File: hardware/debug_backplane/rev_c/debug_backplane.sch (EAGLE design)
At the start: 312 parts, among them J1 BACKPLANE_CONTROLLER_MODULE_D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, J11 PJ-102AH, J12 MICRO_USB_B_HIROSE_ZX62R-B-5P, J2 BACKPLANE_GENERIC_MODULE_DEBUG, J3 BACKPLANE_GENERIC_MODULE_DEBUG, J9 MICRO_USB_B_HIROSE_ZX62R-B-5P, Q1 DMN32D2LDF, Q10 MOSFET-NCHANNELSMD, Q2 DMN32D2LDF, Q3 DMN32D2LDF, Q4 DMN32D2LDF, Q5 DMN32D2LDF, Q6 DMN32D2LDF, U1 FT232RQ, U10 LTC2943, U11 LTC2943, U12 MAX8887EZK33+T, U13 MCP23008QFN, U14 MCP23008QFN, U15 PCA9544AQFN-N20, U16 SAM4LC8AA, U17 SN74LVC2T45, U18 SN74LVC2T45, U19 SN74LVC2T45, U2 FT232RQ, U20 SN74LVC2T45, U21 TS3USB30E, U22 TS3USB30E, U23 TS3USB30E, U24 TUSB2077A, U25 LTC4360, U26 TUSB2077A, U27 FT232RQ, U28 MCP23008QFN, U29 M24C01WMN, U3 FT232RQ, U31 NCP301LSN30, U32 NCP301LSN30, U4 FT232RQ, U5 FT232RQ, U6 FXMA2102, U7 FXMA2102, U8 LTC2943, U9 LTC2943, X1 16MHz, Y1 ABMM, Y2 ABMM

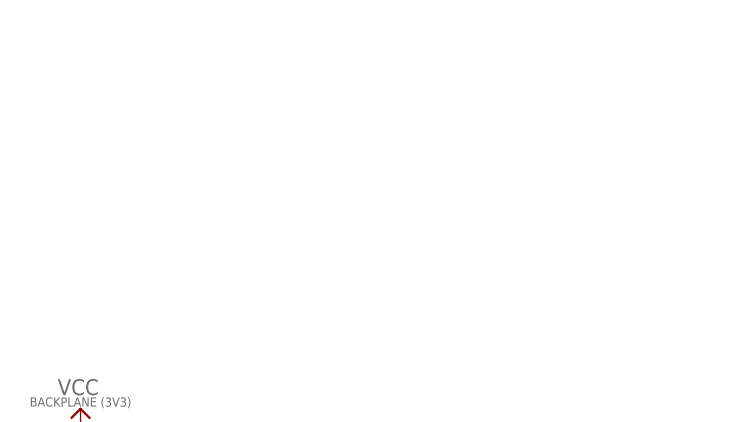
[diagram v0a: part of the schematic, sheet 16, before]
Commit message: debug_backplane: add SMBus header for EEPROM commissioning
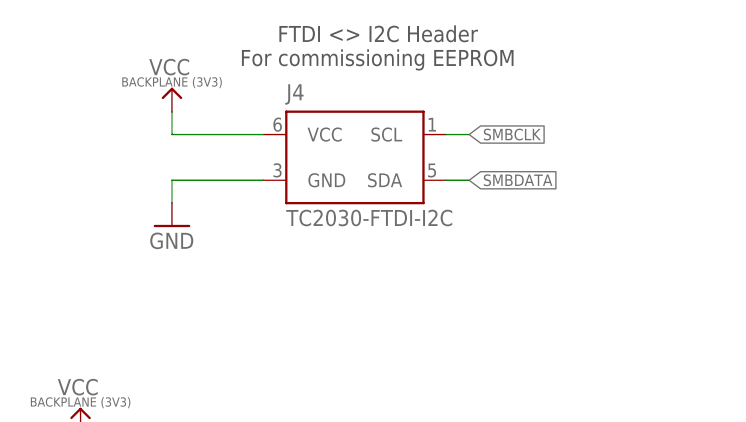
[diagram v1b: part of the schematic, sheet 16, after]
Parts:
- added J4: TC2030-FTDI-I2C, connector:TC2030-FTDI-I2C
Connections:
- net GND: now also J4.GND
- net SMBCLK: now also J4.SCL
- net SMBDATA: now also J4.SDA
- net VCC_BACKPLANE: now also J4.VCC
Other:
- note added: "FTDI <> I2C Header For commissioning EEPROM"
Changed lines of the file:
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@@
 <part name="TP10" library="headers" deviceset="TEST_POINT_0.040IN" device=""/>
 <part name="TP11" library="headers" deviceset="TEST_POINT_0.040IN" device=""/>
+<part name="J4" library="connector" deviceset="TC2030-FTDI-I2C" device=""/>
+<part name="U$74" library="signpost" deviceset="VCC_BACKPLANE" device=""/>
+<part name="GND129" library="umich" deviceset="GND" device=""/>
 </parts>
 <sheets>
@@
 <description>ID EEPROM</description>
 <plain>
+<text x="119.38" y="157.48" size="1.778" layer="97" align="bottom-center">FTDI &lt;&gt; I2C Header
+For commissioning EEPROM</text>
 </plain>
 <instances>
@@
 <attribute name="DIGIKEY" x="86.36" y="96.52" size="1.27" layer="96" align="bottom-center" display="off"/>
 </instance>
+<instance part="J4" gate="G$1" x="116.84" y="147.32"/>
+<instance part="U$74" gate="G$1" x="96.52" y="152.4"/>
+<instance part="GND129" gate="1" x="96.52" y="139.7"/>
 </instances>
 <busses>
@@
 <label x="129.54" y="111.76" size="1.27" layer="95" xref="yes"/>
 </segment>
+<segment>
+<pinref part="J4" gate="G$1" pin="SDA"/>
+<wire x1="129.54" y1="144.78" x2="127" y2="144.78" width="0.1524" layer="91"/>
+<label x="129.54" y="144.78" size="1.27" layer="95" xref="yes"/>
+</segment>
 </net>
 <net name="SMBCLK" class="0">
@@
 <label x="129.54" y="109.22" size="1.27" layer="95" xref="yes"/>
 </segment>
+<segment>
+<pinref part="J4" gate="G$1" pin="SCL"/>
+<wire x1="129.54" y1="149.86" x2="127" y2="149.86" width="0.1524" layer="91"/>
+<label x="129.54" y="149.86" size="1.27" layer="95" xref="yes"/>
+</segment>
 </net>
 <net name="GND" class="0">
@@
 <junction x="104.14" y="96.52"/>
 </segment>
+<segment>
+<pinref part="J4" gate="G$1" pin="GND"/>
+<pinref part="GND129" gate="1" pin="GND"/>
+<wire x1="106.68" y1="144.78" x2="96.52" y2="144.78" width="0.1524" layer="91"/>
+<wire x1="96.52" y1="144.78" x2="96.52" y2="142.24" width="0.1524" layer="91"/>
+</segment>
 </net>
 <net name="VCC_BACKPLANE" class="0">
@@
 <junction x="86.36" y="106.68"/>
 </segment>
+<segment>
+<pinref part="J4" gate="G$1" pin="VCC"/>
+<pinref part="U$74" gate="G$1" pin="VCC_BACKPLANE"/>
+<wire x1="106.68" y1="149.86" x2="96.52" y2="149.86" width="0.1524" layer="91"/>
+<wire x1="96.52" y1="149.86" x2="96.52" y2="152.4" width="0.1524" layer="91"/>
+</segment>
 </net>

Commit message: debug_backplane: add watchdog
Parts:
- added C76: 0.82uF, passives:CAPACITOR0603_CAP
- added C77: 0.47uF, passives:CAPACITOR0603_CAP
- added D36: LED0603, leds:LED0603
- added Q7: DMN32D2LDF, fets:DMN32D2LDF
- added R85: 470Ω, passives:RESISTOR0603_RES
- added R86: 1MΩ, passives:RESISTOR0603_RES
- added S23: TE_SSA12/SPDT, switches:TE_SSA12/SPDT
- added U30: MAX6746, chips:MAX6746
- R17: value 1kΩ -> 470Ω
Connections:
- new net N$65: C76.1, U30.SRT
- new net N$78: Q7.G1, Q7.G2, R86.2, U30.!RESET
- new net N$79: S8.P$2, U30.!MR
- new net N$80: D36.CATHODE, R85.2
- new net N$81: Q7.D1, R85.1
- new net N$82: D3D.CATHODE, Q7.D2
- new net WDT_CTRL: S23.IN, U30.SWT
- new net WDT_ON: C77.1, S23.B
- net !BACKPLANE_RESET: now also D3D.ANODE; no longer S8.P$2
- net !WATCHDOG: now also U30.WDI
- net 3V3_UNMETERED: now also D36.ANODE, U30.VCC, U30.WDS
- net GND: now also C76.2, C77.2, Q7.S, R86.1, S23.A, U30.GND
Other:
- note added: "460nF=300s watchdog timer (extended mode)"
- note added: "800nF = 4s reset period"
- note added: "Connect to GND to disable WDT"

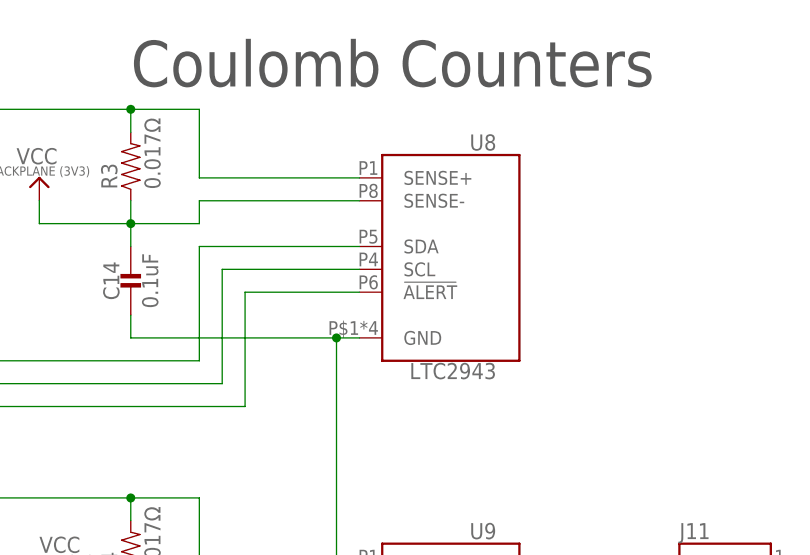
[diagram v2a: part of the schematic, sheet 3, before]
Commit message: debug_backplane: vcc_backplane meter to a 2941
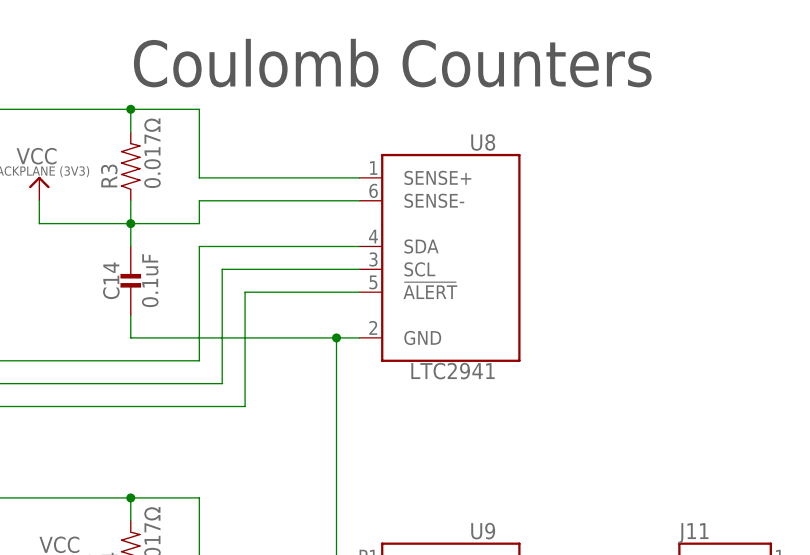
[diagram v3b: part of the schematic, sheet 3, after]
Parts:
- U8: value LTC2943 -> LTC2941; device chips:LTC2943 -> chips:LTC2941
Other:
- moved on the sheet: U8
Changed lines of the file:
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@@
 <part name="TP2" library="headers" deviceset="TEST_POINT_0.040IN" device=""/>
 <part name="TP3" library="headers" deviceset="TEST_POINT_0.040IN" device=""/>
-<part name="U8" library="chips" deviceset="LTC2943" device=""/>
 <part name="U9" library="chips" deviceset="LTC2943" device=""/>
 <part name="U10" library="chips" deviceset="LTC2943" device=""/>
@@
 <attribute name="DIGIKEY" value="490-1539-1-ND"/>
 </part>
+<part name="U8" library="chips" deviceset="LTC2941" device=""/>
 </parts>
 <sheets>
@@
 <instance part="C16" gate="G$1" x="111.76" y="76.2"/>
 <instance part="C17" gate="G$1" x="111.76" y="33.02"/>
-<instance part="U8" gate="G$1" x="137.16" y="165.1" rot="MR0"/>
 <instance part="U9" gate="G$1" x="137.16" y="121.92" rot="MR0"/>
 <instance part="U10" gate="G$1" x="137.16" y="78.74" rot="MR0"/>
 <instance part="U11" gate="G$1" x="137.16" y="35.56" rot="MR0"/>
+<instance part="U8" gate="G$1" x="137.16" y="165.1" rot="MR0"/>
 </instances>
 <busses>
@@
 <pinref part="C16" gate="G$1" pin="2"/>
 <pinref part="C17" gate="G$1" pin="2"/>
-<pinref part="U8" gate="G$1" pin="GND"/>
 <pinref part="U11" gate="G$1" pin="GND"/>
 <pinref part="U10" gate="G$1" pin="GND"/>
 <pinref part="U9" gate="G$1" pin="GND"/>
-</segment>
-<segment>
+<pinref part="U8" gate="G$1" pin="GND"/>
+</segment>
+<segment>

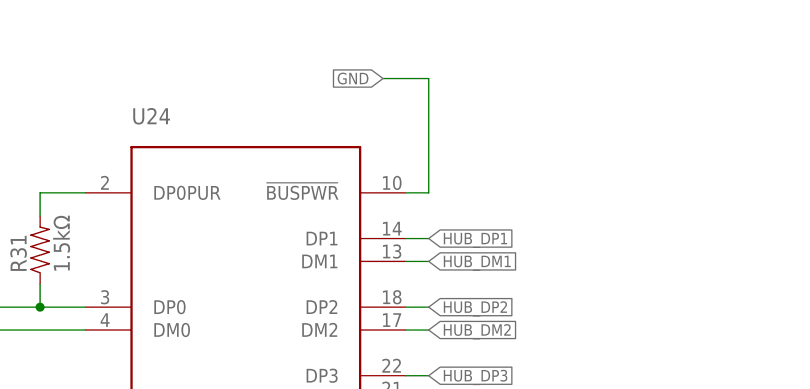
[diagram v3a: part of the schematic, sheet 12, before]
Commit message: debug_backplane: module hub !BUSPWR -> high
mirros the d43e926 fix to the backplane
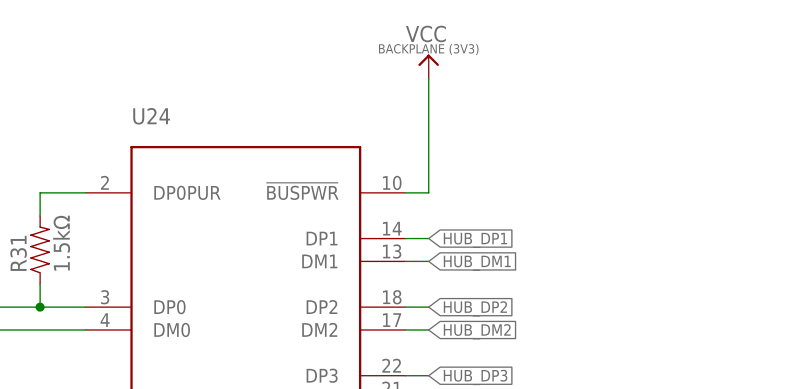
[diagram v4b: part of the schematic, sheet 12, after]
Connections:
- net GND: no longer U24.!BUSPWR
- net VCC_BACKPLANE: now also U24.!BUSPWR
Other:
- note added: "This hub &downstream ports are "externally" powered (not limited to 500mA from host)"
- note removed: "Downstream ports draw VBUS from the "cable""
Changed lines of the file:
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@@
 <?xml version="1.0" encoding="utf-8"?>
 <!DOCTYPE eagle SYSTEM "eagle.dtd">
-<eagle version="8.2.0">
+<eagle version="8.2.2">
 <drawing>
 <settings>
@@
 <part name="R86" library="passives" deviceset="RESISTOR" device="0603_RES" value="1MΩ"/>
 <part name="C76" library="passives" deviceset="CAPACITOR" device="0603_CAP" value="0.82uF">
-<attribute name="DIGIKEY" value="	490-11493-1-ND"/>
+<attribute name="DIGIKEY" value=" 490-11493-1-ND"/>
 </part>
 <part name="C77" library="passives" deviceset="CAPACITOR" device="0603_CAP" value="0.47uF">
@@
 </part>
 <part name="U8" library="chips" deviceset="LTC2941" device=""/>
+<part name="U$77" library="signpost" deviceset="VCC_BACKPLANE" device=""/>
 </parts>
 <sheets>
@@
 <wire x1="40.64" y1="73.66" x2="40.64" y2="63.5" width="0.1524" layer="98"/>
 <wire x1="40.64" y1="63.5" x2="68.58" y2="63.5" width="0.1524" layer="98"/>
-<text x="93.98" y="167.64" size="1.27" layer="98">Downstream ports draw
-VBUS from the "cable"</text>
+<text x="88.9" y="167.64" size="1.27" layer="98">This hub &amp;downstream ports
+are "externally" powered
+(not limited to 500mA from host)</text>
 <text x="53.34" y="119.38" size="1.27" layer="98">!EXTMEM -&gt; high, no mem
 !GANGED -&gt; high, OVR per port
@@
 <instance part="R52" gate="G$1" x="22.86" y="119.38" rot="R90"/>
 <instance part="U$22" gate="G$1" x="17.78" y="127"/>
+<instance part="U$77" gate="G$1" x="114.3" y="172.72"/>
 </instances>
 <busses>
@@
 <net name="GND" class="0">
 <segment>
-<pinref part="U24" gate="G$1" pin="!BUSPWR"/>
-<wire x1="111.76" y1="160.02" x2="114.3" y2="160.02" width="0.1524" layer="91"/>
-<wire x1="114.3" y1="160.02" x2="114.3" y2="172.72" width="0.1524" layer="91"/>
-<wire x1="114.3" y1="172.72" x2="109.22" y2="172.72" width="0.1524" layer="91"/>
-<label x="109.22" y="172.72" size="1.27" layer="95" rot="R180" xref="yes"/>
-</segment>
-<segment>
 <pinref part="U24" gate="G$1" pin="GND"/>
 <pinref part="GND15" gate="1" pin="GND"/>
@@
 <pinref part="U$22" gate="G$1" pin="VCC_BACKPLANE"/>
 </segment>
+<segment>
+<pinref part="U$77" gate="G$1" pin="VCC_BACKPLANE"/>
+<wire x1="114.3" y1="172.72" x2="114.3" y2="160.02" width="0.1524" layer="91"/>
+<pinref part="U24" gate="G$1" pin="!BUSPWR"/>
+<wire x1="114.3" y1="160.02" x2="111.76" y2="160.02" width="0.1524" layer="91"/>
+</segment>
 </net>

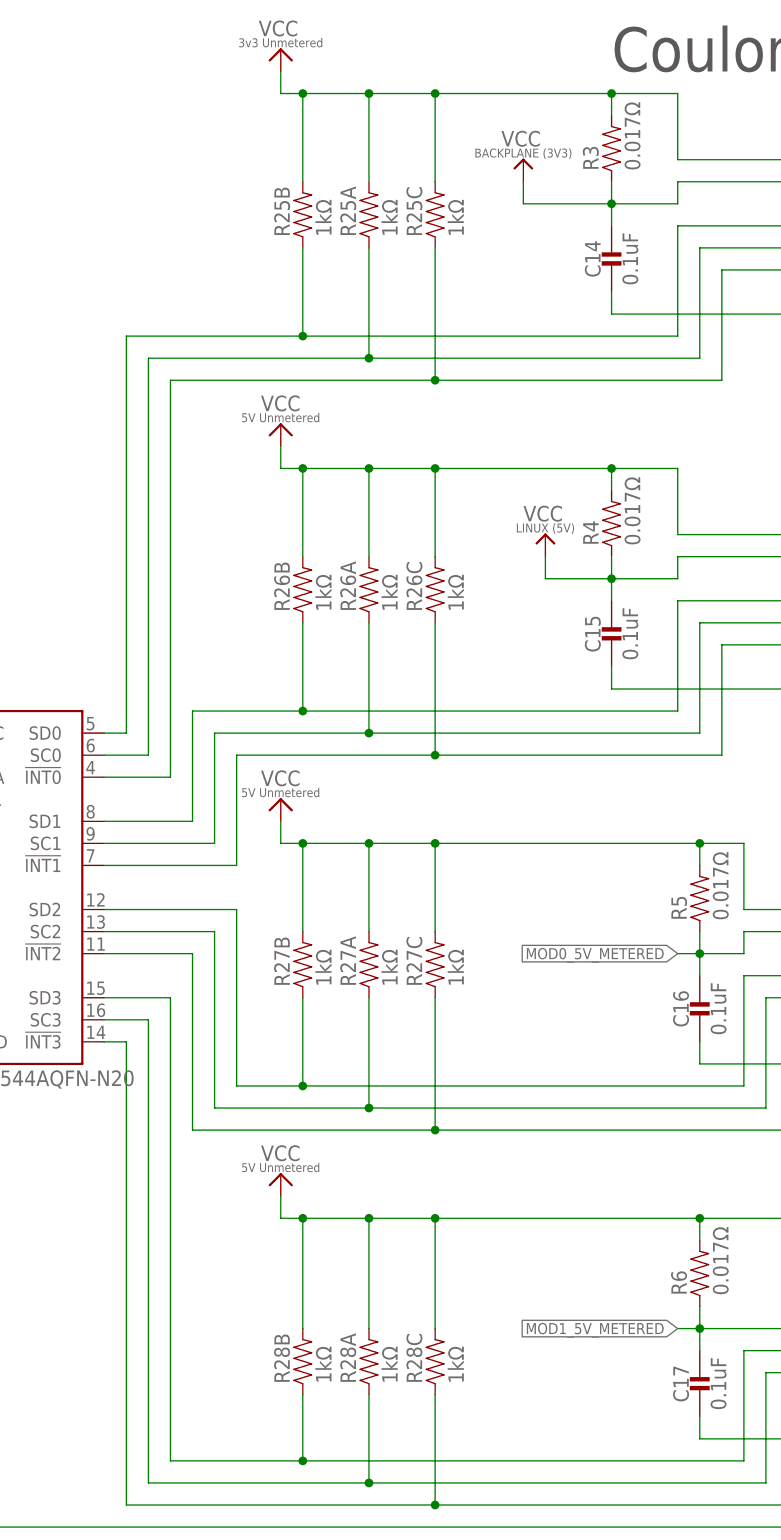
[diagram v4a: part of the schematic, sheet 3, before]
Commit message: debug_backplane: 1k -> 1.8k R on coulomb counters
2k chip resistors are non-stock, need to choose between 1.8 and 2.2
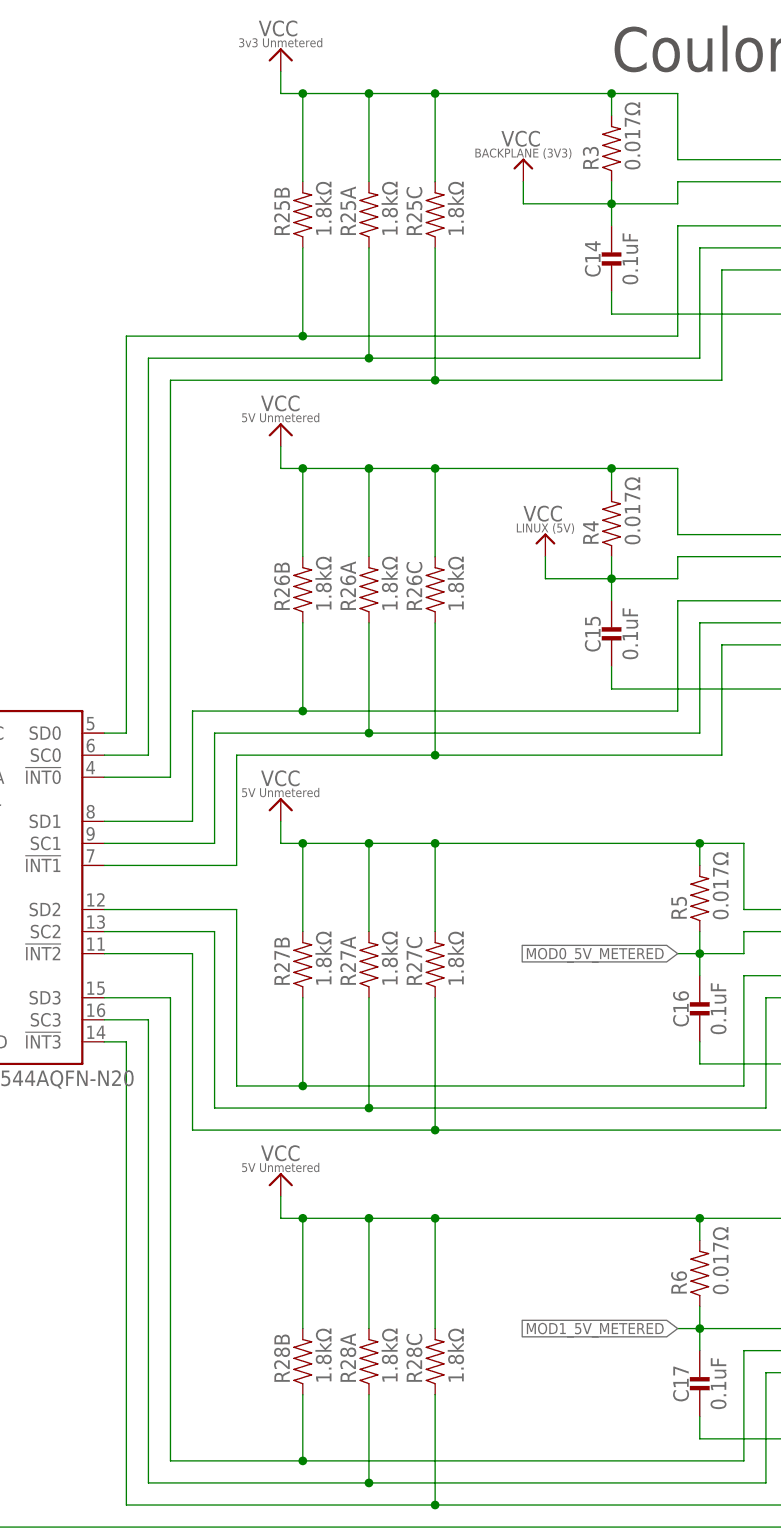
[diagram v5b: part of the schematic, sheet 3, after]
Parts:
- R25, R26, R27, R28: value 1kΩ -> 1.8kΩ; DIGIKEY Y9102CT-ND -> Y9182CT-ND
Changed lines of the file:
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@@
 <attribute name="DIGIKEY" value="Y9102CT-ND"/>
 </part>
-<part name="R25" library="passives" deviceset="RESISTOR-ARRAY-4" device="1206" value="1kΩ">
-<attribute name="DIGIKEY" value="Y9102CT-ND"/>
+<part name="R25" library="passives" deviceset="RESISTOR-ARRAY-4" device="1206" value="1.8kΩ">
+<attribute name="DIGIKEY" value="Y9182CT-ND"/>
 </part>
-<part name="R26" library="passives" deviceset="RESISTOR-ARRAY-4" device="1206" value="1kΩ">
-<attribute name="DIGIKEY" value="Y9102CT-ND"/>
+<part name="R26" library="passives" deviceset="RESISTOR-ARRAY-4" device="1206" value="1.8kΩ">
+<attribute name="DIGIKEY" value="Y9182CT-ND"/>
 </part>
-<part name="R27" library="passives" deviceset="RESISTOR-ARRAY-4" device="1206" value="1kΩ">
-<attribute name="DIGIKEY" value="Y9102CT-ND"/>
+<part name="R27" library="passives" deviceset="RESISTOR-ARRAY-4" device="1206" value="1.8kΩ">
+<attribute name="DIGIKEY" value="Y9182CT-ND"/>
 </part>
-<part name="R28" library="passives" deviceset="RESISTOR-ARRAY-4" device="1206" value="1kΩ">
-<attribute name="DIGIKEY" value="Y9102CT-ND"/>
+<part name="R28" library="passives" deviceset="RESISTOR-ARRAY-4" device="1206" value="1.8kΩ">
+<attribute name="DIGIKEY" value="Y9182CT-ND"/>
 </part>
 <part name="C13" library="passives" deviceset="CAPACITOR" device="0603_CAP" value="0.01uF"/>

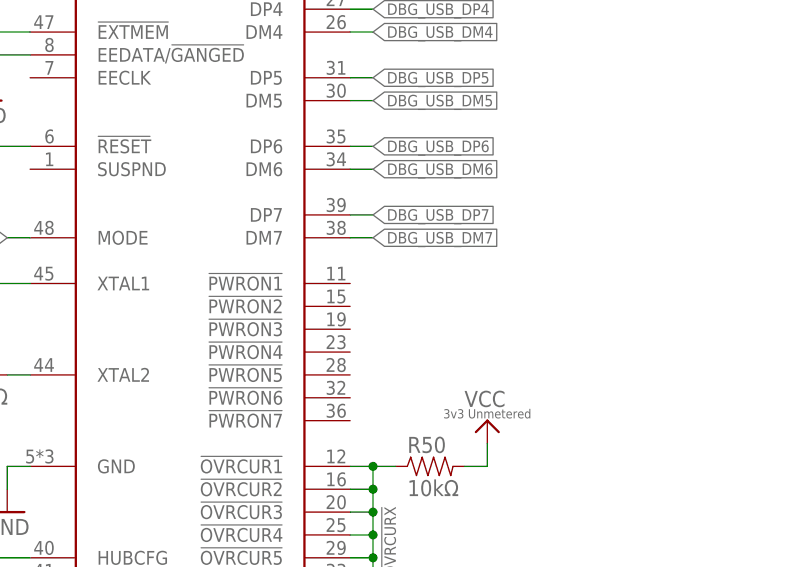
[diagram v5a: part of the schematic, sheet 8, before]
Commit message: debug_backplane: add !PWRON testpoint for debug hub
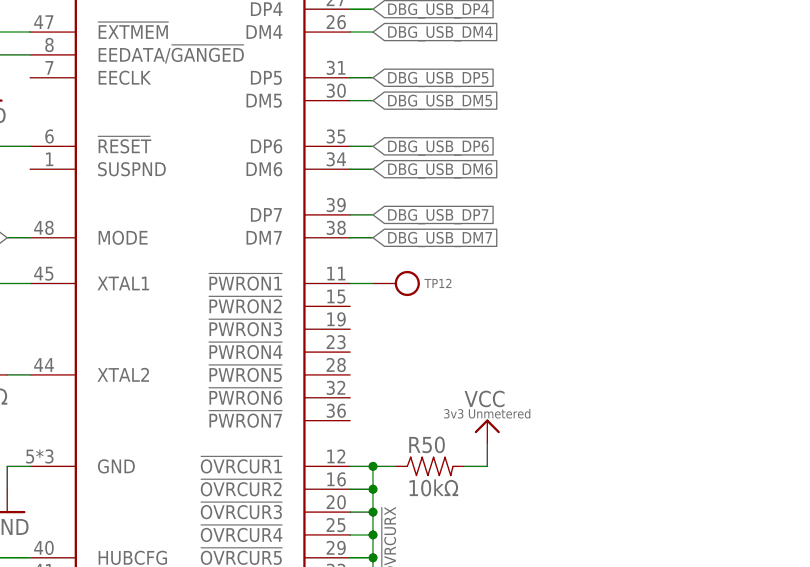
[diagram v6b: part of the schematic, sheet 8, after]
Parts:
- added TP12: TEST_POINT_0.040IN, headers:TEST_POINT_0.040IN
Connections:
- new net DBG_USB_!PWRON: TP12.TESTPOINT, U26.!PWRON1
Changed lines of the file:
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@@
 <part name="U8" library="chips" deviceset="LTC2941" device=""/>
 <part name="U$77" library="signpost" deviceset="VCC_BACKPLANE" device=""/>
+<part name="TP12" library="headers" deviceset="TEST_POINT_0.040IN" device=""/>
 </parts>
 <sheets>
@@
 <instance part="TP2" gate="G$1" x="63.5" y="50.8"/>
 <instance part="TP3" gate="G$1" x="63.5" y="48.26"/>
+<instance part="TP12" gate="G$1" x="134.62" y="83.82" rot="R180"/>
 </instances>
 <busses>
@@
 </segment>
 </net>
+<net name="DBG_USB_!PWRON" class="0">
+<segment>
+<pinref part="TP12" gate="G$1" pin="TESTPOINT"/>
+<pinref part="U26" gate="G$1" pin="!PWRON1"/>
+<wire x1="132.08" y1="83.82" x2="129.54" y2="83.82" width="0.1524" layer="91"/>
+</segment>
+</net>
